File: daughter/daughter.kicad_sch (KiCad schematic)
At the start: 2 parts, among them U1 ESP32-C3, Y1 Crystal_GND24_Small

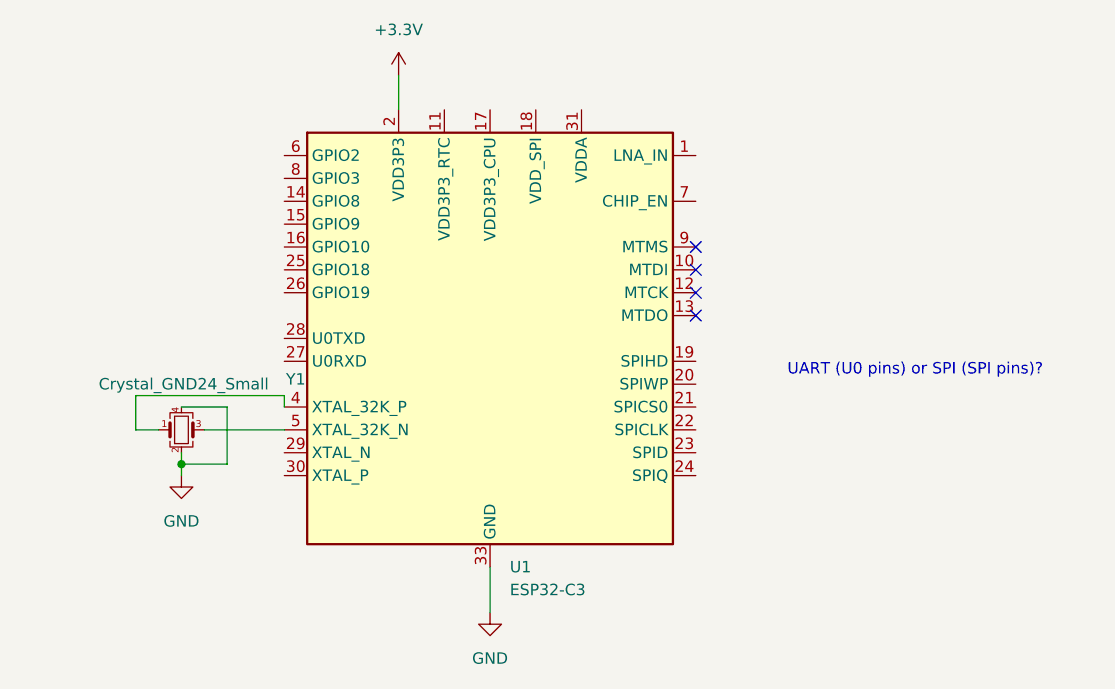
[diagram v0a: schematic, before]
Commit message: Added components
Added pressure sensor (placeholder MS5837) and note that we need MOSFET for power relay. Added power relay component: G5LE.
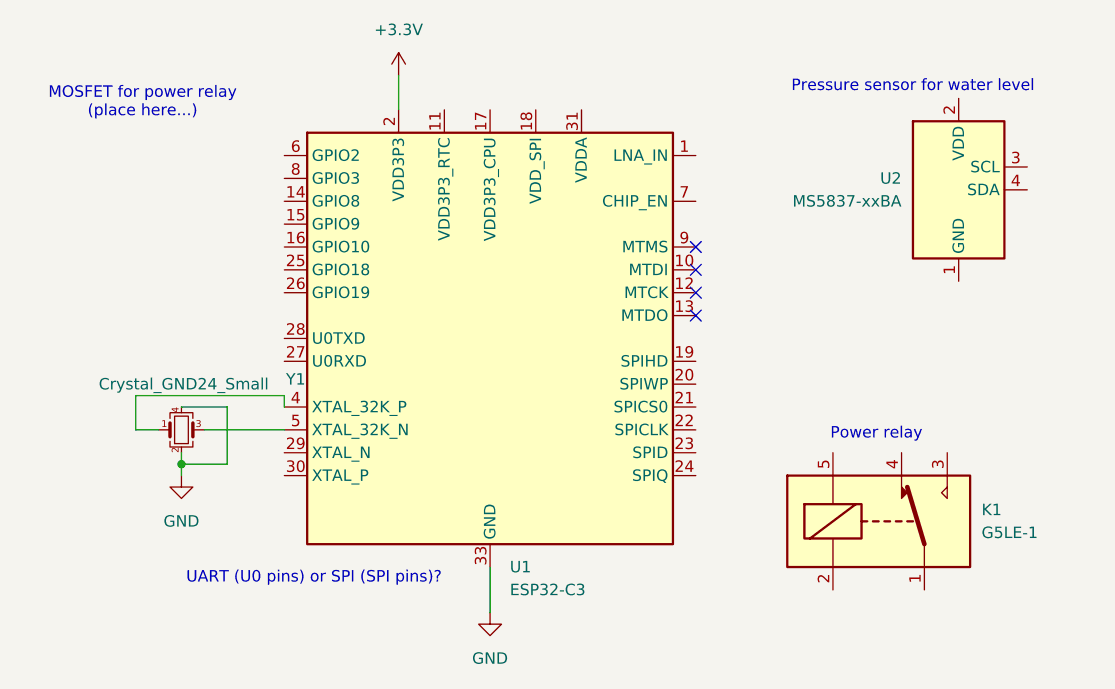
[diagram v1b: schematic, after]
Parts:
- added K1: G5LE-1, Relay_THT:Relay_SPDT_Omron-G5LE-1, symbol Relay:G5LE-1
- added U2: MS5837-xxBA, Sensor_Pressure:TE_MS5837-xxBA, symbol Sensor_Pressure:MS5837-xxBA
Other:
- note added: "MOSFET for power relay (place here...)"
- note added: "Power relay"
- note added: "Pressure sensor for water level"
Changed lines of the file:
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@@
+		)
+	)
+	(text "MOSFET for power relay\n(place here...)"
+		(exclude_from_sim no)
+		(at 103.632 72.898 0)
+		(effects
+			(font
+				(size 1.27 1.27)
+			)
+		)
+	)
+	(text "Power relay"
+		(exclude_from_sim no)
+		(at 185.166 109.728 0)
+		(effects
+			(font
+				(size 1.27 1.27)
+			)
+		)
+	)
+	(text "Pressure sensor for water level"
+		(exclude_from_sim no)
+		(at 189.23 71.12 0)
+		(effects
+			(font
+				(size 1.27 1.27)
+			)
 		)
 	)
 	(text "UART (U0 pins) or SPI (SPI pins)?"
 		(exclude_from_sim no)
-		(at 189.484 102.616 0)
+		(at 122.682 125.73 0)
 		(effects
 			(font
@@
 					(unit 1)
 				)
+			)
+		)
+	)
+	(symbol
+		(lib_id "Relay:G5LE-1")
+		(at 185.42 119.38 0)
+		(unit 1)
+		(exclude_from_sim no)
+		(in_bom yes)
+		(on_board yes)
+		(dnp no)
+		(fields_autoplaced yes)
+		(property "Reference" "K1"
+			(at 196.85 118.1099 0)
+			(effects
+				(font
+					(size 1.27 1.27)
+				)
+				(justify left)
+			)
+		)
+		(property "Value" "G5LE-1"
+			(at 196.85 120.6499 0)
+			(effects
+				(font
+					(size 1.27 1.27)
+				)
+				(justify left)
+			)
+		)
+		(property "Footprint" "Relay_THT:Relay_SPDT_Omron-G5LE-1"
+			(at 196.85 120.65 0)
+			(effects
+				(font
+					(size 1.27 1.27)
+				)
+				(justify left)
+				(hide yes)
+			)
+		)
+		(property "Datasheet" "http://www.omron.com/ecb/products/pdf/en-g5le.pdf"
+			(at 185.42 119.38 0)
+			(effects
+				(font
+					(size 1.27 1.27)
+				)
+				(hide yes)
+			)
+		)
+		(property "Description" "Omron G5LE relay, Miniature Single Pole, SPDT, 10A"
+			(at 185.42 119.38 0)
+			(effects
+				(font
+					(size 1.27 1.27)
+				)
+				(hide yes)
+			)
+		)
+		(pin "2"
+		)
+		(pin "3"
+		)
+		(pin "4"
+		)
+		(pin "5"
+		)
+		(pin "1"
+		)
+		(instances
+			(project ""
+				(path "/9e050361-84ba-4b41-8bc1-d0f304e5538b"
+					(reference "K1")
+					(unit 1)
+				)
+			)
+		)
+	)
+	(symbol
+		(lib_id "Sensor_Pressure:MS5837-xxBA")
+		(at 194.31 82.55 0)
+		(unit 1)
+		(exclude_from_sim no)
+		(in_bom yes)
+		(on_board yes)
+		(dnp no)
+		(fields_autoplaced yes)
+		(property "Reference" "U2"
+			(at 187.96 81.2799 0)
+			(effects
+				(font
+					(size 1.27 1.27)
+				)
+				(justify right)
+			)
+		)
+		(property "Value" "MS5837-xxBA"
+			(at 187.96 83.8199 0)
+			(effects
+				(font
+					(size 1.27 1.27)
+				)
+				(justify right)
+			)
+		)
+		(property "Footprint" "Sensor_Pressure:TE_MS5837-xxBA"
+			(at 194.31 82.55 0)
+			(effects
+				(font
+					(size 1.27 1.27)
+				)
+				(hide yes)
+			)
+		)
+		(property "Datasheet" "https://www.te.com/commerce/DocumentDelivery/DDEController?Action=showdoc&DocId=Data+Sheet%7FMS5837-30BA%7FB1%7Fpdf%7FEnglish%7FENG_DS_MS5837-30BA_B1.pdf%7FCAT-BLPS0017"
+			(at 194.31 85.09 0)
+			(effects
+				(font
+					(size 1.27 1.27)
+				)
+				(hide yes)
+			)
+		)
+		(property "Description" "Ultra-small, gel-filled, pressure sensor with stainless steel cap"
+			(at 194.31 82.55 0)
+			(effects
+				(font
+					(size 1.27 1.27)
+				)
+				(hide yes)
+			)
+		)
+		(pin "1"
+		)
+		(pin "2"
+		)
+		(pin "3"
+		)
+		(pin "4"
+		)
+		(instances
+			(project ""
+				(path "/9e050361-84ba-4b41-8bc1-d0f304e5538b"
+					(reference "U2")
+					(unit 1)
+				)
